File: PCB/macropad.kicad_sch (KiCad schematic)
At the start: 40 parts, among them SW1 Kailh Choc V2, SW10 Kailh Choc V2, SW11 Kailh Choc V2, SW12 Kailh Choc V2, SW13 Kailh Choc V2, SW14 Kailh Choc V2, SW15 Kailh Choc V2, SW16 Kailh Choc V2, SW2 Kailh Choc V2, SW3 Kailh Choc V2, SW4 Kailh Choc V2, SW5 Kailh Choc V2, SW6 Kailh Choc V2, SW7 Kailh Choc V2, SW8 Kailh Choc V2, SW9 Kailh Choc V2, U2 SEEEDUINO XIAO RP2040

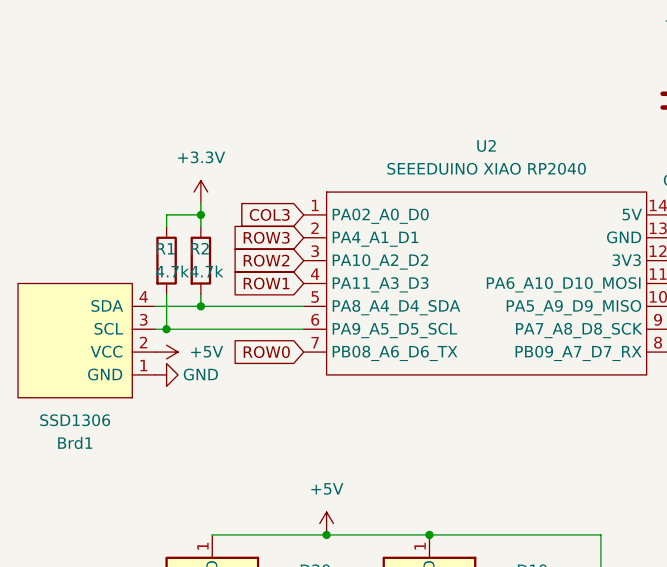
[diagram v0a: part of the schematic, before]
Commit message: Revamp switch margins
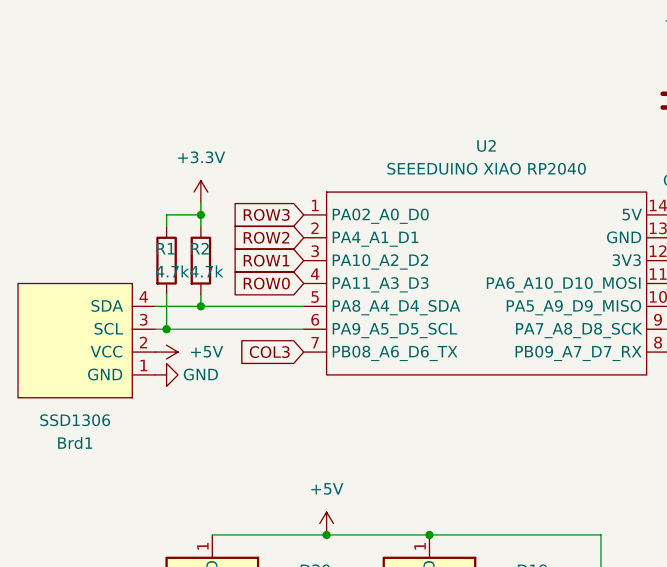
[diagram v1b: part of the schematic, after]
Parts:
- SW1, SW10, SW11, SW12, SW13, SW14, SW15, SW16, SW2, SW3, SW4, SW5, SW6, SW7, SW8, SW9: footprint key:SW_Kailh_Choc_V2 -> key:SW_Kailh_Choc_V2_1.00u
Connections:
- net COL3: now also U2.7 (PB08_A6_D6_TX); no longer U2.1 (PA02_A0_D0)
- net ROW0: now also U2.4 (PA11_A3_D3); no longer U2.7 (PB08_A6_D6_TX)
- net ROW1: now also U2.3 (PA10_A2_D2); no longer U2.4 (PA11_A3_D3)
- net ROW2: now also U2.2 (PA4_A1_D1); no longer U2.3 (PA10_A2_D2)
- net ROW3: now also U2.1 (PA02_A0_D0); no longer U2.2 (PA4_A1_D1)
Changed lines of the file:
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@@
     )
   )
-  (global_label "ROW0" (shape input) (at 91.44 96.52 180) (fields_autoplaced)
+  (global_label "ROW0" (shape input) (at 91.44 88.9 180) (fields_autoplaced)
     (effects (font (size 1.27 1.27)) (justify right))
-    (property "Intersheetrefs" "${INTERSHEET_REFS}" (at 83.1934 96.52 0)
+    (property "Intersheetrefs" "${INTERSHEET_REFS}" (at 83.1934 88.9 0)
       (effects (font (size 1.27 1.27)) (justify right) hide)
     )
@@
     )
   )
-  (global_label "COL3" (shape input) (at 91.44 81.28 180) (fields_autoplaced)
+  (global_label "COL3" (shape input) (at 91.44 96.52 180) (fields_autoplaced)
     (effects (font (size 1.27 1.27)) (justify right))
-    (property "Intersheetrefs" "${INTERSHEET_REFS}" (at 83.6167 81.28 0)
+    (property "Intersheetrefs" "${INTERSHEET_REFS}" (at 83.6167 96.52 0)
       (effects (font (size 1.27 1.27)) (justify right) hide)
     )
   )
-  (global_label "ROW1" (shape input) (at 91.44 88.9 180) (fields_autoplaced)
+  (global_label "ROW1" (shape input) (at 91.44 86.36 180) (fields_autoplaced)
     (effects (font (size 1.27 1.27)) (justify right))
-    (property "Intersheetrefs" "${INTERSHEET_REFS}" (at 83.1934 88.9 0)
+    (property "Intersheetrefs" "${INTERSHEET_REFS}" (at 83.1934 86.36 0)
       (effects (font (size 1.27 1.27)) (justify right) hide)
     )
   )
-  (global_label "ROW3" (shape input) (at 91.44 83.82 180) (fields_autoplaced)
+  (global_label "ROW3" (shape input) (at 91.44 81.28 180) (fields_autoplaced)
     (effects (font (size 1.27 1.27)) (justify right))
-    (property "Intersheetrefs" "${INTERSHEET_REFS}" (at 83.1934 83.82 0)
+    (property "Intersheetrefs" "${INTERSHEET_REFS}" (at 83.1934 81.28 0)
       (effects (font (size 1.27 1.27)) (justify right) hide)
     )
@@
     )
   )
-  (global_label "ROW2" (shape input) (at 91.44 86.36 180) (fields_autoplaced)
+  (global_label "ROW2" (shape input) (at 91.44 83.82 180) (fields_autoplaced)
     (effects (font (size 1.27 1.27)) (justify right))
-    (property "Intersheetrefs" "${INTERSHEET_REFS}" (at 83.1934 86.36 0)
+    (property "Intersheetrefs" "${INTERSHEET_REFS}" (at 83.1934 83.82 0)
       (effects (font (size 1.27 1.27)) (justify right) hide)
     )
@@
       (effects (font (size 1.27 1.27)))
     )
-    (property "Footprint" "key:SW_Kailh_Choc_V2" (at 181.61 72.39 0)
+    (property "Footprint" "key:SW_Kailh_Choc_V2_1.00u" (at 181.61 72.39 0)
       (effects (font (size 1.27 1.27)) hide)
     )
@@
       (effects (font (size 1.27 1.27)))
     )
-    (property "Footprint" "key:SW_Kailh_Choc_V2" (at 217.17 72.39 0)
+    (property "Footprint" "key:SW_Kailh_Choc_V2_1.00u" (at 217.17 72.39 0)
       (effects (font (size 1.27 1.27)) hide)
     )
@@
       (effects (font (size 1.27 1.27)))
     )
-    (property "Footprint" "key:SW_Kailh_Choc_V2" (at 181.61 93.98 0)
+    (property "Footprint" "key:SW_Kailh_Choc_V2_1.00u" (at 181.61 93.98 0)
       (effects (font (size 1.27 1.27)) hide)
     )
@@
       (effects (font (size 1.27 1.27)))
     )
-    (property "Footprint" "key:SW_Kailh_Choc_V2" (at 217.17 115.57 0)
+    (property "Footprint" "key:SW_Kailh_Choc_V2_1.00u" (at 217.17 115.57 0)
       (effects (font (size 1.27 1.27)) hide)
     )
@@
       (effects (font (size 1.27 1.27)))
     )
-    (property "Footprint" "key:SW_Kailh_Choc_V2" (at 217.17 93.98 0)
+    (property "Footprint" "key:SW_Kailh_Choc_V2_1.00u" (at 217.17 93.98 0)
       (effects (font (size 1.27 1.27)) hide)
     )
@@
       (effects (font (size 1.27 1.27)))
     )
-    (property "Footprint" "key:SW_Kailh_Choc_V2" (at 163.83 93.98 0)
+    (property "Footprint" "key:SW_Kailh_Choc_V2_1.00u" (at 163.83 93.98 0)
       (effects (font (size 1.27 1.27)) hide)
     )
@@
       (effects (font (size 1.27 1.27)))
     )
-    (property "Footprint" "key:SW_Kailh_Choc_V2" (at 199.39 50.8 0)
+    (property "Footprint" "key:SW_Kailh_Choc_V2_1.00u" (at 199.39 50.8 0)
       (effects (font (size 1.27 1.27)) hide)
     )
@@
       (effects (font (size 1.27 1.27)))
     )
-    (property "Footprint" "key:SW_Kailh_Choc_V2" (at 163.83 72.39 0)
+    (property "Footprint" "key:SW_Kailh_Choc_V2_1.00u" (at 163.83 72.39 0)
       (effects (font (size 1.27 1.27)) hide)
     )
@@
       (effects (font (size 1.27 1.27)))
     )
-    (property "Footprint" "key:SW_Kailh_Choc_V2" (at 181.61 115.57 0)
+    (property "Footprint" "key:SW_Kailh_Choc_V2_1.00u" (at 181.61 115.57 0)
       (effects (font (size 1.27 1.27)) hide)
     )
@@
       (effects (font (size 1.27 1.27)))
     )
-    (property "Footprint" "key:SW_Kailh_Choc_V2" (at 199.39 115.57 0)
+    (property "Footprint" "key:SW_Kailh_Choc_V2_1.00u" (at 199.39 115.57 0)
       (effects (font (size 1.27 1.27)) hide)
     )
@@
       (effects (font (size 1.27 1.27)))
     )
-    (property "Footprint" "key:SW_Kailh_Choc_V2" (at 181.61 50.8 0)
+    (property "Footprint" "key:SW_Kailh_Choc_V2_1.00u" (at 181.61 50.8 0)
       (effects (font (size 1.27 1.27)) hide)
     )
@@
       (effects (font (size 1.27 1.27)))
     )
-    (property "Footprint" "key:SW_Kailh_Choc_V2" (at 199.39 72.39 0)
+    (property "Footprint" "key:SW_Kailh_Choc_V2_1.00u" (at 199.39 72.39 0)
       (effects (font (size 1.27 1.27)) hide)
     )
@@
       (effects (font (size 1.27 1.27)))
     )
-    (property "Footprint" "key:SW_Kailh_Choc_V2" (at 199.39 93.98 0)
+    (property "Footprint" "key:SW_Kailh_Choc_V2_1.00u" (at 199.39 93.98 0)
       (effects (font (size 1.27 1.27)) hide)
     )
@@
       (effects (font (size 1.27 1.27)))
     )
-    (property "Footprint" "key:SW_Kailh_Choc_V2" (at 217.17 50.8 0)
+    (property "Footprint" "key:SW_Kailh_Choc_V2_1.00u" (at 217.17 50.8 0)
       (effects (font (size 1.27 1.27)) hide)
     )
@@
       (effects (font (size 1.27 1.27)))
     )
-    (property "Footprint" "key:SW_Kailh_Choc_V2" (at 163.83 115.57 0)
+    (property "Footprint" "key:SW_Kailh_Choc_V2_1.00u" (at 163.83 115.57 0)
       (effects (font (size 1.27 1.27)) hide)
     )
@@
       (effects (font (size 1.27 1.27)))
     )
-    (property "Footprint" "key:SW_Kailh_Choc_V2" (at 163.83 50.8 0)
-      (effects (font (size 1.27 1.27)) hide)
-    )
+    (property "Footprint" "key:SW_Kailh_Choc_V2_1.00u" (at 163.83 50.8 0)
+      (effects (font (size 1.27 1.27)) hide)
+    )

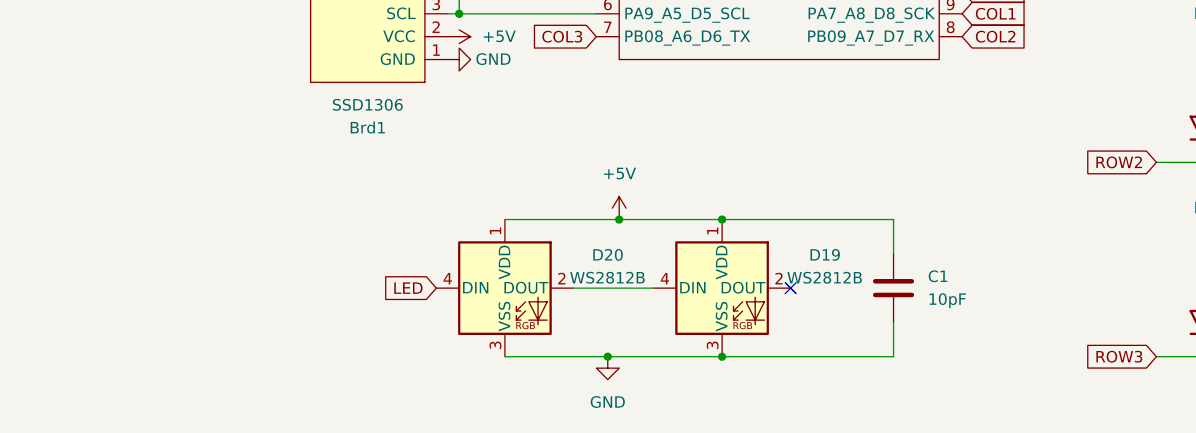
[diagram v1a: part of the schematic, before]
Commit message: Added backlights
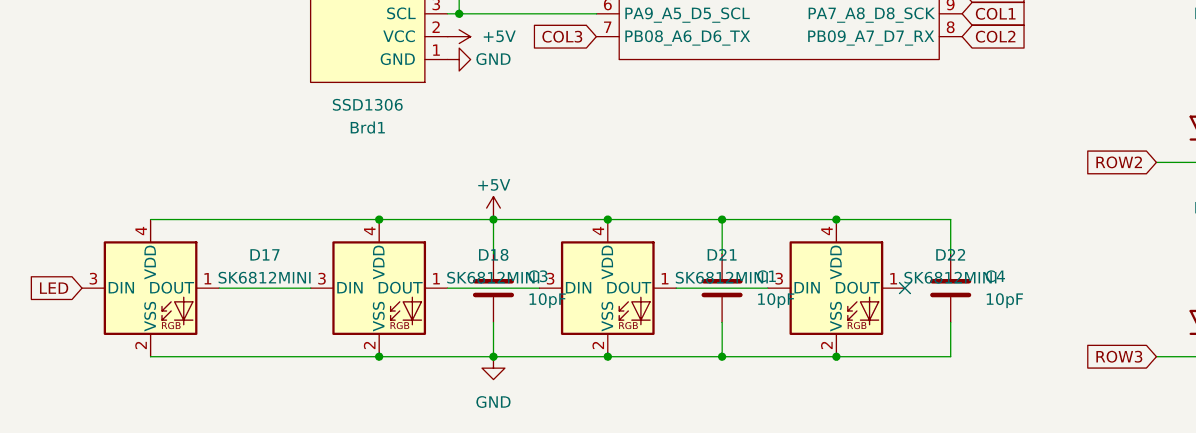
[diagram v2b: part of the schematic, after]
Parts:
- removed D19, D20: WS2812B, LED_SMD:LED_WS2812B_PLCC4_5.0x5.0mm_P3.2mm, symbol LED:WS2812B
- added C3, C4: 10pF, Capacitor_THT:C_Disc_D3.0mm_W1.6mm_P2.50mm, symbol Device:C
- added D17, D18, D21, D22: SK6812MINI, LED:SK6812MINI-E, symbol LED:SK6812MINI
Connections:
- net +5V: now also C3.1, C4.1, D17.4 (VDD), D18.4 (VDD), D21.4 (VDD), D22.4 (VDD)
- net GND: now also C3.2, C4.2, D17.2 (VSS), D18.2 (VSS), D21.2 (VSS), D22.2 (VSS)
- net LED: now also D17.3 (DIN)
- new net: D21.1 (DOUT), D22.3 (DIN)
- new net: D18.1 (DOUT), D21.3 (DIN)
- new net: D17.1 (DOUT), D18.3 (DIN)

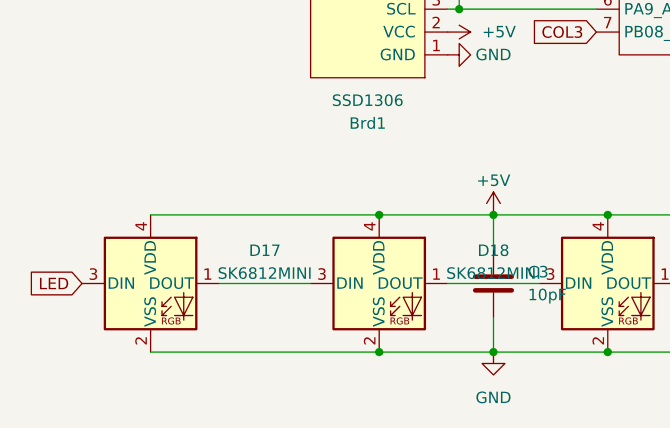
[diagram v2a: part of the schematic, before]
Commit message: Add silkscreens and misc improvements
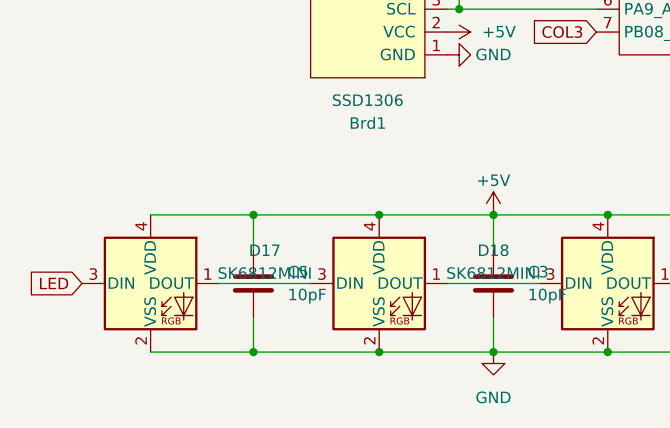
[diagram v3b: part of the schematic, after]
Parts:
- added C5: 10pF, Capacitor_THT:C_Disc_D3.0mm_W1.6mm_P2.50mm, symbol Device:C
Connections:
- net +5V: now also C5.1
- net GND: now also C5.2
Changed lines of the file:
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@@
   (junction (at 80.01 116.84) (diameter 0) (color 0 0 0 0)
   )
+  (junction (at 53.34 132.08) (diameter 0) (color 0 0 0 0)
+  )
   (junction (at 222.25 55.88) (diameter 0) (color 0 0 0 0)
   )
@@
   )
   (junction (at 194.31 67.31) (diameter 0) (color 0 0 0 0)
+  )
+  (junction (at 53.34 116.84) (diameter 0) (color 0 0 0 0)
   )
   (junction (at 80.01 91.44) (diameter 0) (color 0 0 0 0)
@@
     (stroke (width 0) (type default))
   )
+  (wire (pts (xy 53.34 128.27) (xy 53.34 132.08))
+    (stroke (width 0) (type default))
+  )
+  (wire (pts (xy 53.34 116.84) (xy 67.31 116.84))
+    (stroke (width 0) (type default))
+  )
   (wire (pts (xy 194.31 120.65) (xy 194.31 124.46))
     (stroke (width 0) (type default))
@@
     (stroke (width 0) (type default))
   )
+  (wire (pts (xy 53.34 116.84) (xy 53.34 120.65))
+    (stroke (width 0) (type default))
+  )
   (wire (pts (xy 194.31 110.49) (xy 212.09 110.49))
     (stroke (width 0) (type default))
@@
     (stroke (width 0) (type default))
   )
-  (wire (pts (xy 41.91 132.08) (xy 67.31 132.08))
+  (wire (pts (xy 41.91 132.08) (xy 53.34 132.08))
     (stroke (width 0) (type default))
   )
@@
     (stroke (width 0) (type default))
   )
-  (wire (pts (xy 41.91 116.84) (xy 67.31 116.84))
+  (wire (pts (xy 41.91 116.84) (xy 53.34 116.84))
     (stroke (width 0) (type default))
   )
@@
   )
   (wire (pts (xy 92.71 132.08) (xy 105.41 132.08))
+    (stroke (width 0) (type default))
+  )
+  (wire (pts (xy 53.34 132.08) (xy 67.31 132.08))
     (stroke (width 0) (type default))
   )
@@
         )
       )
+    )
+  )
+  (symbol (lib_id "Device:C") (at 53.34 124.46 0) (unit 1)
+    (in_bom yes) (on_board yes) (dnp no) (fields_autoplaced)
+    (property "Reference" "C5" (at 57.15 123.19 0)
+      (effects (font (size 1.27 1.27)) (justify left))
+    )
+    (property "Value" "10pF" (at 57.15 125.73 0)
+      (effects (font (size 1.27 1.27)) (justify left))
+    )
+    (property "Footprint" "Capacitor_THT:C_Disc_D3.0mm_W1.6mm_P2.50mm" (at 54.3052 128.27 0)
+      (effects (font (size 1.27 1.27)) hide)
+    )
+    (property "Datasheet" "~" (at 53.34 124.46 0)
+      (effects (font (size 1.27 1.27)) hide)
+    )
+    (pin "1")
+    (pin "2")
+    (instances
+      (project "macropad"
+        (path "/bbfb2475-963d-4c49-ac81-fadef0dd23d7"
+          (reference "C5") (unit 1)
+        )
+      )

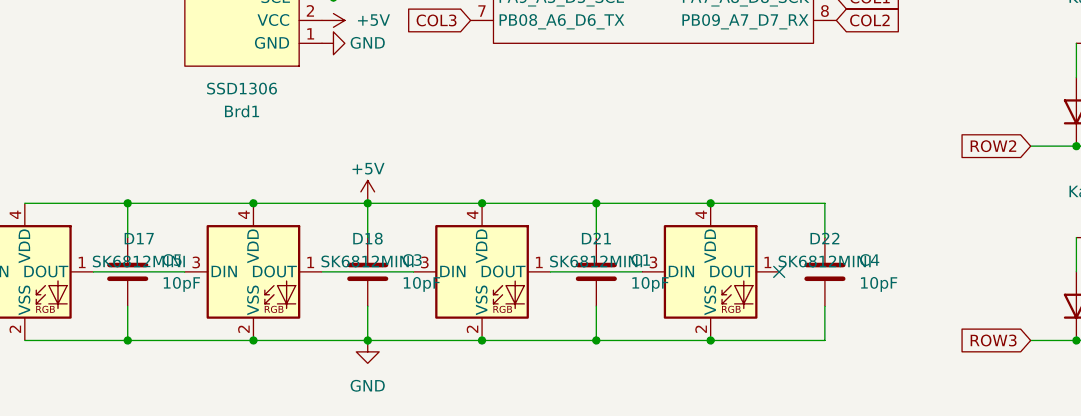
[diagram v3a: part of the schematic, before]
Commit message: Change capacitor values and positions
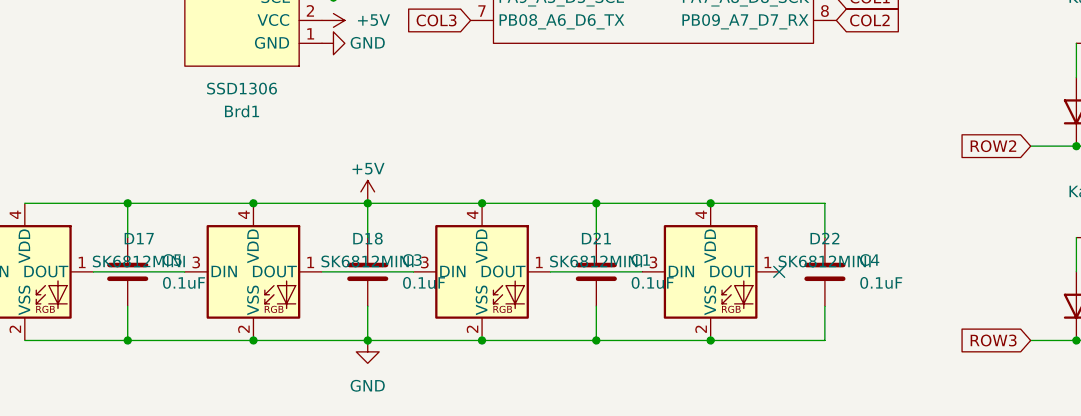
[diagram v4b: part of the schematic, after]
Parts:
- C1, C3, C4, C5: value 10pF -> 0.1uF
